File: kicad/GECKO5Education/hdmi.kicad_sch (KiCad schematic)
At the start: 14 parts, among them J2 HDMI_A, J6 Conn_01x06_Socket, J7 Conn_01x02_Pin, U16 LTC2632CTS8-LZ12TRMPBF, U17 MAX11666AUBV, U6 LFE5U-85F-6BG381x

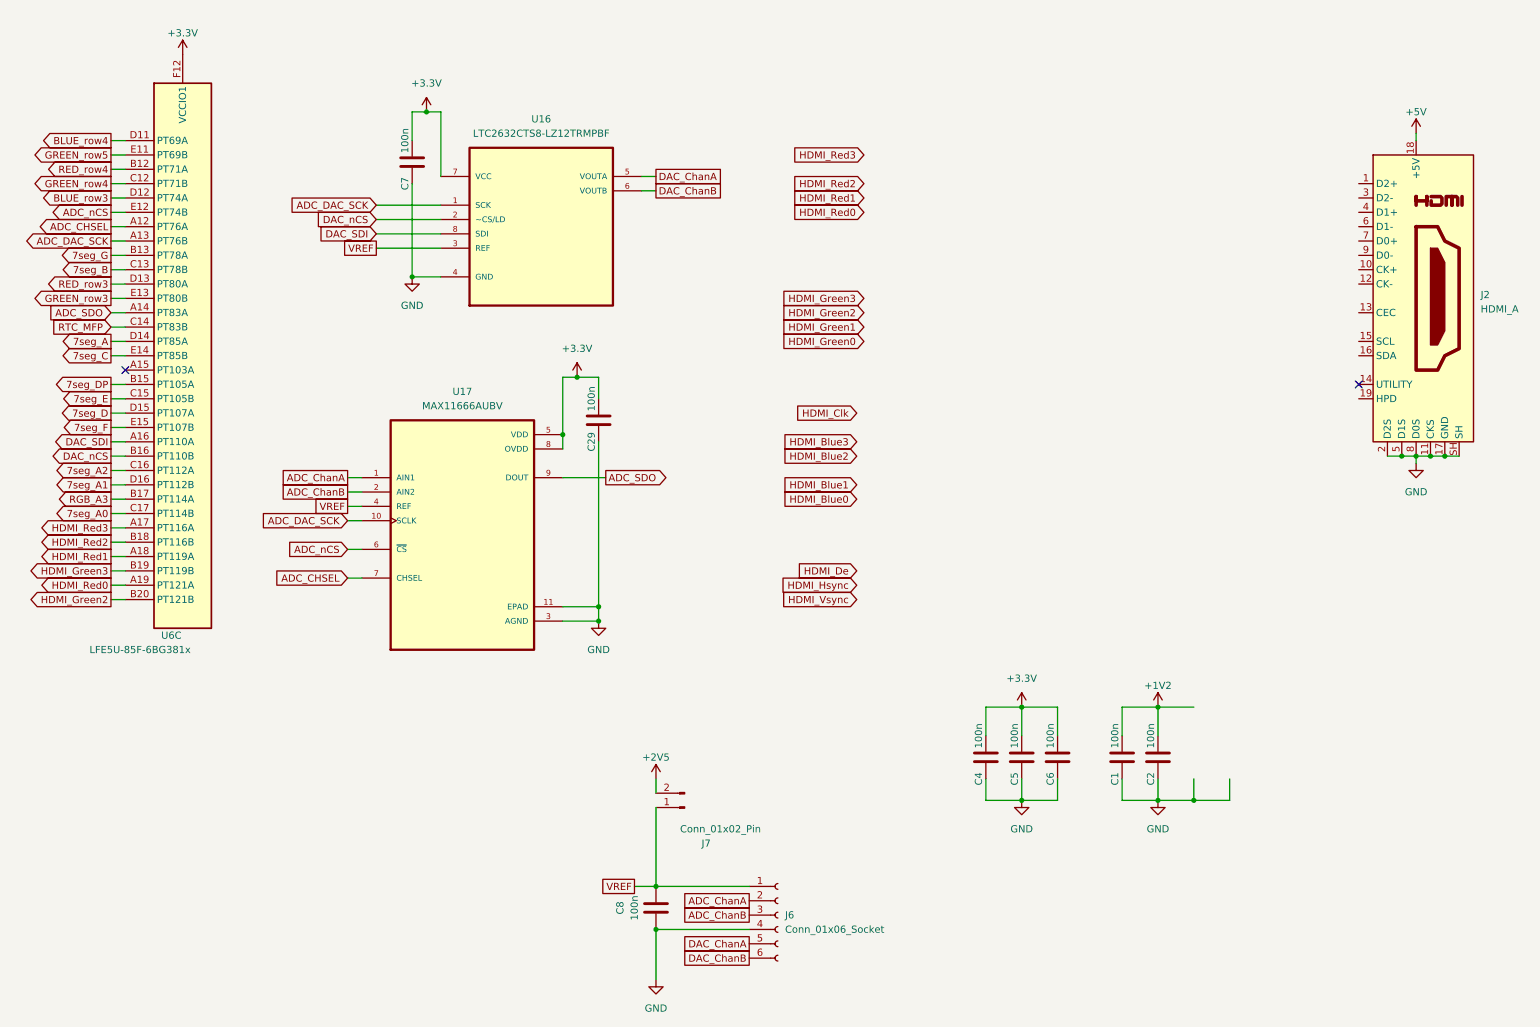
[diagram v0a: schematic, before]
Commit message: Added chip
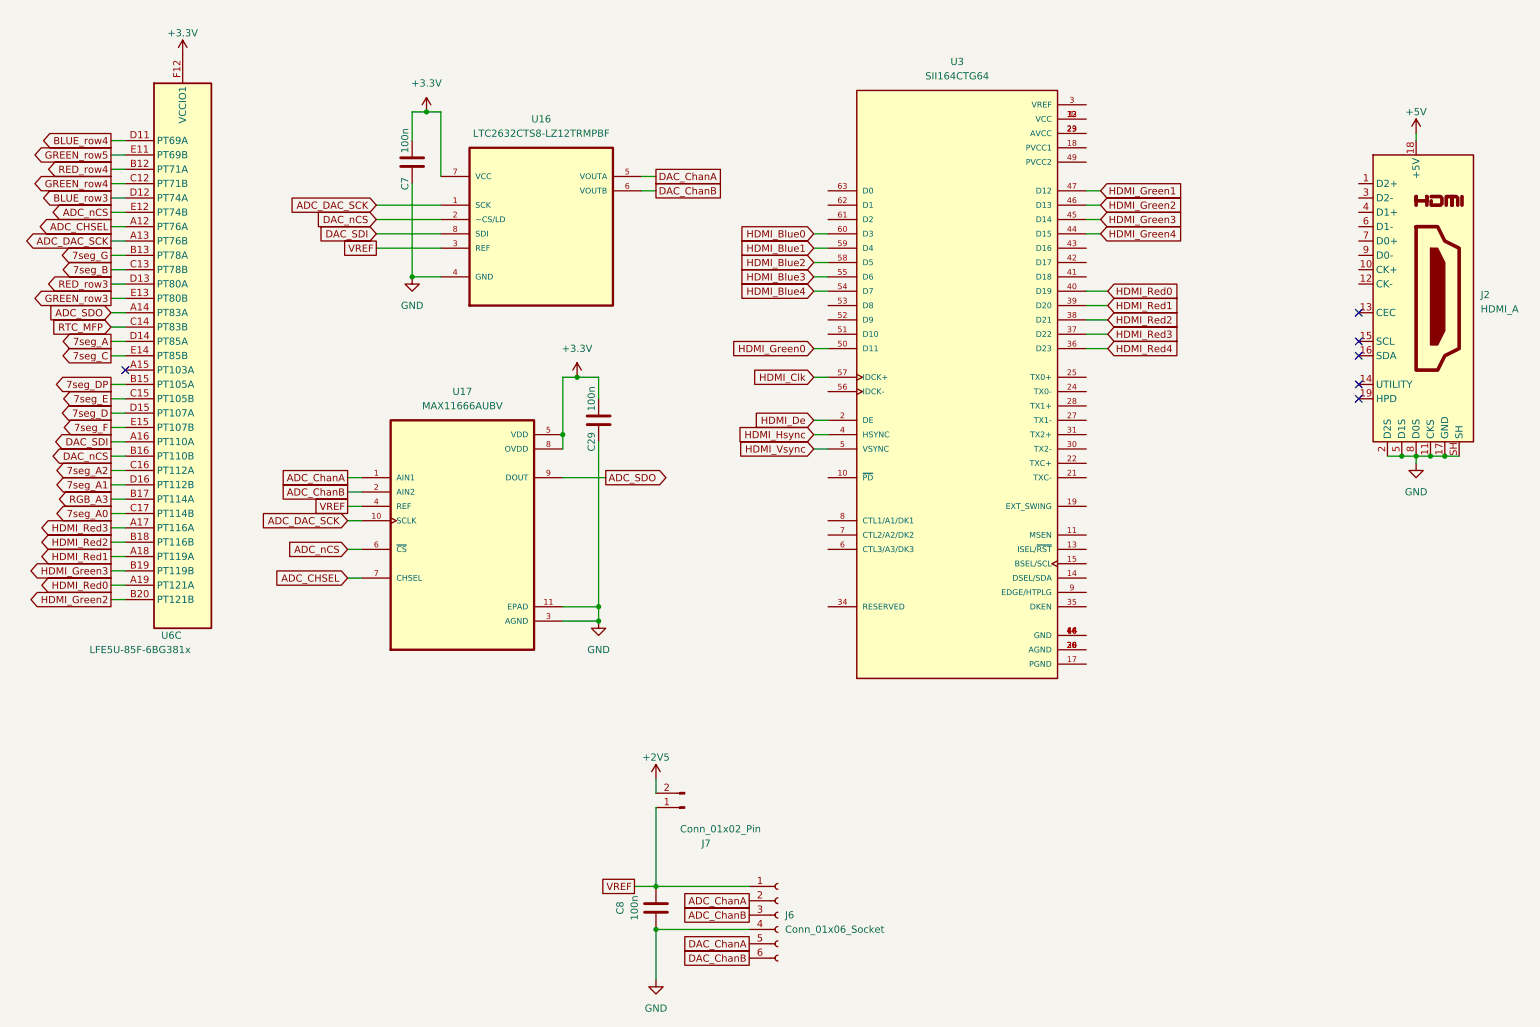
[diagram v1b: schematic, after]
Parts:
- removed C1, C2, C4, C5, C6: 100n, Resistor_SMD:R_0402_1005Metric, symbol Device:C
- added U3: SII164CTG64, gecko4education:QFP50P1200X1200X120-64N, symbol gecko5education:SII164CTG64
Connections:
- net HDMI_Blue0: now also U3.60 (D3)
- net HDMI_Blue1: now also U3.59 (D4)
- net HDMI_Blue2: now also U3.58 (D5)
- net HDMI_Blue3: now also U3.55 (D6)
- net HDMI_Clk: now also U3.57 (IDCK+)
- net HDMI_De: now also U3.2 (DE)
- net HDMI_Green0: now also U3.50 (D11)
- net HDMI_Green1: now also U3.47 (D12)
- net HDMI_Green2: now also U3.46 (D13)
- net HDMI_Green3: now also U3.45 (D14)
- net HDMI_Hsync: now also U3.4 (HSYNC)
- net HDMI_Red0: now also U3.40 (D19)
- net HDMI_Red1: now also U3.39 (D20)
- net HDMI_Red2: now also U3.38 (D21)
- net HDMI_Red3: now also U3.37 (D22)
- net HDMI_Vsync: now also U3.5 (VSYNC)
- new net: U3.1 (VCC), U3.12 (VCC), U3.33 (VCC)
- new net: U3.16 (GND), U3.48 (GND), U3.64 (GND)
- new net: U3.20 (AGND), U3.26 (AGND), U3.32 (AGND)
- new net: U3.23 (AVCC), U3.29 (AVCC)
- new net HDMI_Blue4: U3.54 (D7)
- new net HDMI_Green4: U3.44 (D15)
- new net HDMI_Red4: U3.36 (D23)
- no-connect marks 2 -> 6

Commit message: Final version
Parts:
- added C1, C2, C3, C4: 100n, Resistor_SMD:R_0402_1005Metric, symbol Device:C
- added R10, R11, R12, R13, R14, R7: 10k, Resistor_SMD:R_0402_1005Metric, symbol Device:R
- added R8: 510R, Resistor_SMD:R_0402_1005Metric, symbol Device:R
- renumbered J6 to J3
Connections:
- net +3.3V: now also U3.1 (VCC), U3.12 (VCC), U3.18 (PVCC1), U3.23 (AVCC), U3.29 (AVCC), U3.3 (VREF), U3.33 (VCC), U3.49 (PVCC2), C1.2, C2.2, C3.2, C4.2, R11.2, R13.2, R7.1, R8.2
- net GND: now also U3.16 (GND), U3.17 (PGND), U3.20 (AGND), U3.26 (AGND), U3.32 (AGND), U3.34 (RESERVED), U3.41 (D18), U3.42 (D17), U3.43 (D16), U3.48 (GND), U3.51 (D10), U3.52 (D9), U3.53 (D8), U3.56 (IDCK-), U3.6 (CTL3/A3/DK3), U3.61 (D2), U3.62 (D1), U3.63 (D0), U3.64 (GND), U3.7 (CTL2/A2/DK2), U3.8 (CTL1/A1/DK1), C1.1, C2.1, C3.1, C4.1, R10.2, R12.2, R14.2
- net HDMI_Green2: no longer U6.B20 (PT121B)
- net HDMI_Green3: no longer U6.B19 (PT119B)
- net HDMI_Green4: now also U6.B20 (PT121B)
- net HDMI_Red0: now also U6.B19 (PT119B); no longer U6.A19 (PT121A)
- net HDMI_Red1: now also U6.A19 (PT121A); no longer U6.A18 (PT119A)
- net HDMI_Red3: now also U6.A18 (PT119A); no longer U6.A17 (PT116A)
- net HDMI_Red4: now also U6.A17 (PT116A)
- net TX2+: now reaches J2.1 (D2+)
- net TX2+: now also U3.31 (TX2+)
- net TXC+: now reaches J2.10 (CK+)
- net TXC+: now also U3.22 (TXC+)
- net TXC-: now reaches J2.12 (CK-)
- net TXC-: now also U3.21 (TXC-)
- net TX2-: now reaches J2.3 (D2-)
- net TX2-: now also U3.30 (TX2-)
- net TX1+: now reaches J2.4 (D1+)
- net TX1+: now also U3.28 (TX1+)
- net TX1-: now reaches J2.6 (D1-)
- net TX1-: now also U3.27 (TX1-)
- net TX0+: now reaches J2.7 (D0+)
- net TX0+: now also U3.25 (TX0+)
- net TX0-: now reaches J2.9 (D0-)
- net TX0-: now also U3.24 (TX0-)
- net at U3.10 (~{PD}): now also R7.2
- net at U3.13 (ISEL/~{RST}): now also R10.1
- net at U3.14 (DSEL/SDA): now also R12.1
- net at U3.15 (BSEL/SCL): now also R11.1
- net at U3.19 (EXT_SWING): now also R8.1
- net at U3.35 (DKEN): now also R14.1
- net at U3.9 (EDGE/HTPLG): now also R13.1
- no-connect marks 6 -> 7

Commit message: Cleaned up
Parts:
- U3: value SII164CTG64 -> TFP410PAP
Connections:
- net GND: now also U3.65 (Termal_pad)
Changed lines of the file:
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@@
   (junction (at 242.57 31.75) (diameter 0) (color 0 0 0 0)
+  )
+  (junction (at 158.75 124.46) (diameter 0) (color 0 0 0 0)
   )
   (junction (at 266.7 95.25) (diameter 0) (color 0 0 0 0)
@@
     (stroke (width 0) (type default))
   )
+  (wire (pts (xy 158.75 124.46) (xy 160.02 124.46))
+    (stroke (width 0) (type default))
+  )
   (wire (pts (xy 242.57 31.75) (xy 240.03 31.75))
     (stroke (width 0) (type default))
@@
     (stroke (width 0) (type default))
   )
-  (wire (pts (xy 158.75 121.92) (xy 158.75 135.89))
+  (wire (pts (xy 158.75 121.92) (xy 158.75 124.46))
     (stroke (width 0) (type default))
   )
@@
   )
   (wire (pts (xy 91.44 63.5) (xy 86.36 63.5))
+    (stroke (width 0) (type default))
+  )
+  (wire (pts (xy 158.75 124.46) (xy 158.75 135.89))
     (stroke (width 0) (type default))
   )
@@
       (effects (font (size 1.27 1.27)))
     )
-    (property "Value" "SII164CTG64" (at 182.88 27.94 0)
+    (property "Value" "TFP410PAP" (at 182.88 27.94 0)
       (effects (font (size 1.27 1.27)))
     )
@@
     (pin "15")
     (pin "60")
-    (instances
-      (project "gecko5education"
+    (pin "65")
+    (instances
+      (project "gecko5education"

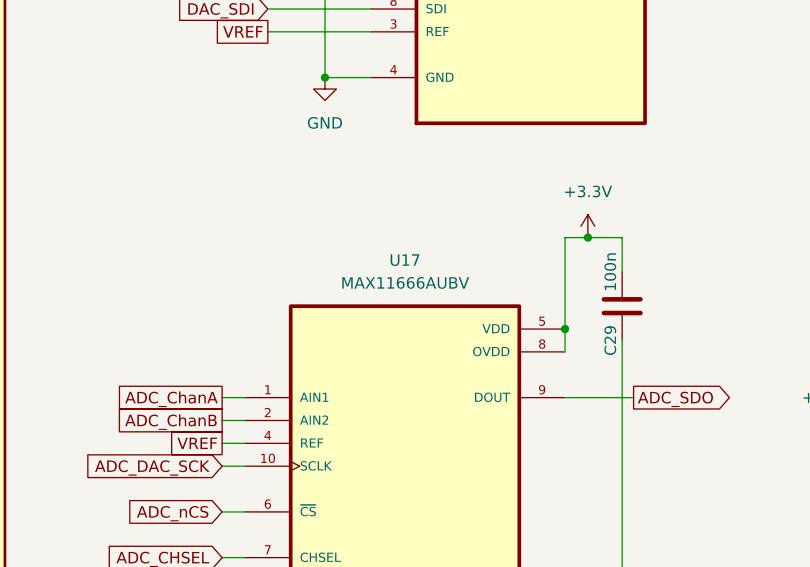
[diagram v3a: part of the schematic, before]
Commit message: Added faster AD-converter. Changed "System Reset" into "Board Reset"
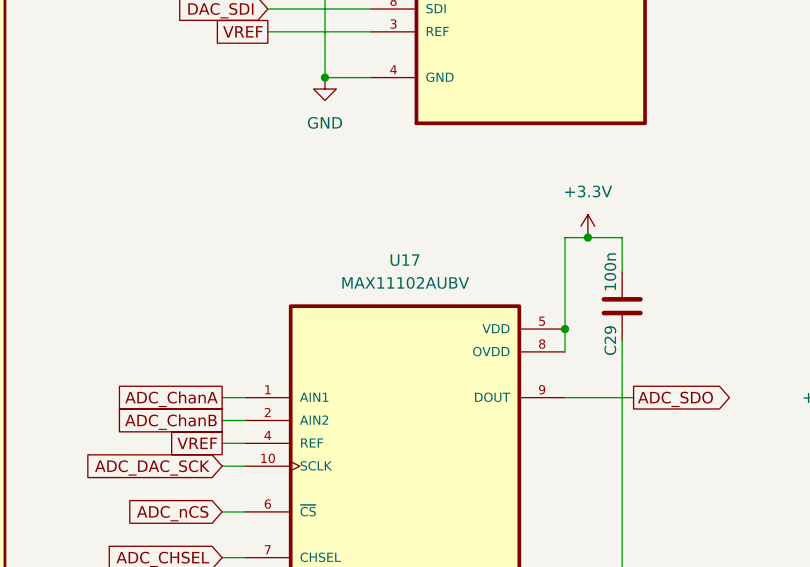
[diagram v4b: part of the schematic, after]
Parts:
- U17: value MAX11666AUBV -> MAX11102AUBV
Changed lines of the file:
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@@
       (effects (font (size 1.27 1.27)))
     )
-    (property "Value" "MAX11666AUBV" (at 95.25 86.36 0)
+    (property "Value" "MAX11102AUBV" (at 95.25 86.36 0)
       (effects (font (size 1.27 1.27)))
     )
